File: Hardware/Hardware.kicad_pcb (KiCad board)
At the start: 2 copper layers, 58.4 x 30.5 mm, 16 parts, among them J1 Conn_01x02, J2 Conn_01x04, J3 Conn_01x06, J4 Conn_01x02, J7 Conn_01x03, U1 ESP32-WROOM-32

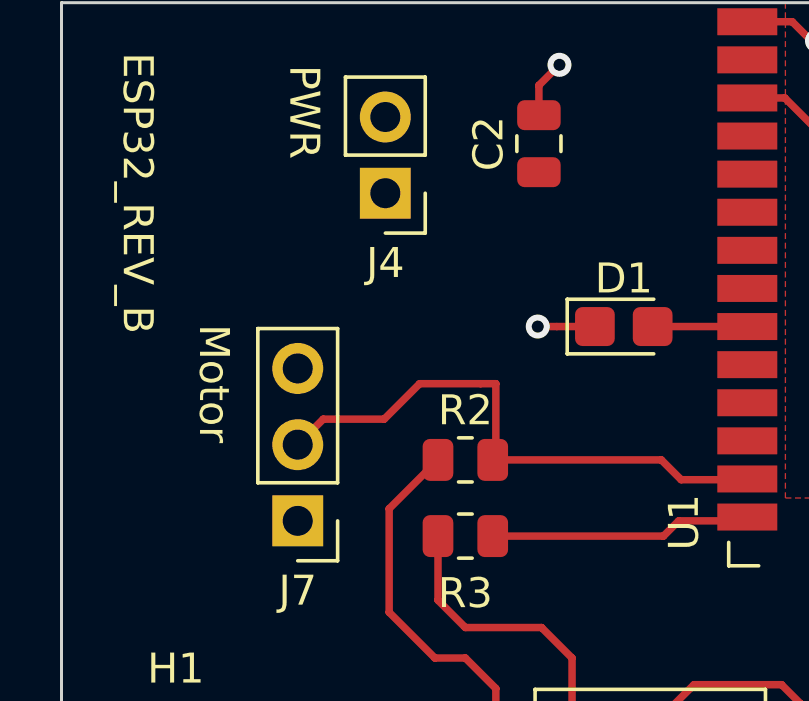
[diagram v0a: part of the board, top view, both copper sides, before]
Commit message: Servo pin fix
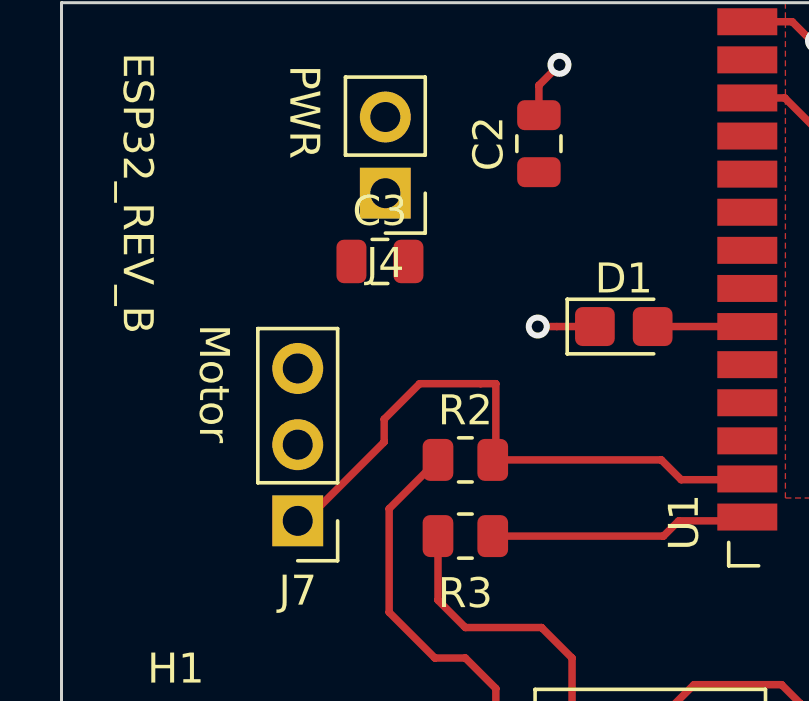
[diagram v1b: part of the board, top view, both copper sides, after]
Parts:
- added C3: 0.1uF, Capacitor_SMD:C_0805_2012Metric, F.Cu at (90.6, 105.1)
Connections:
- J7 pad 1: /VDD33 -> /MTMS
- J7 pad 2: /MTMS -> /VDD33
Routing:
- net /MTMS: track 18.6 -> 19.6 mm

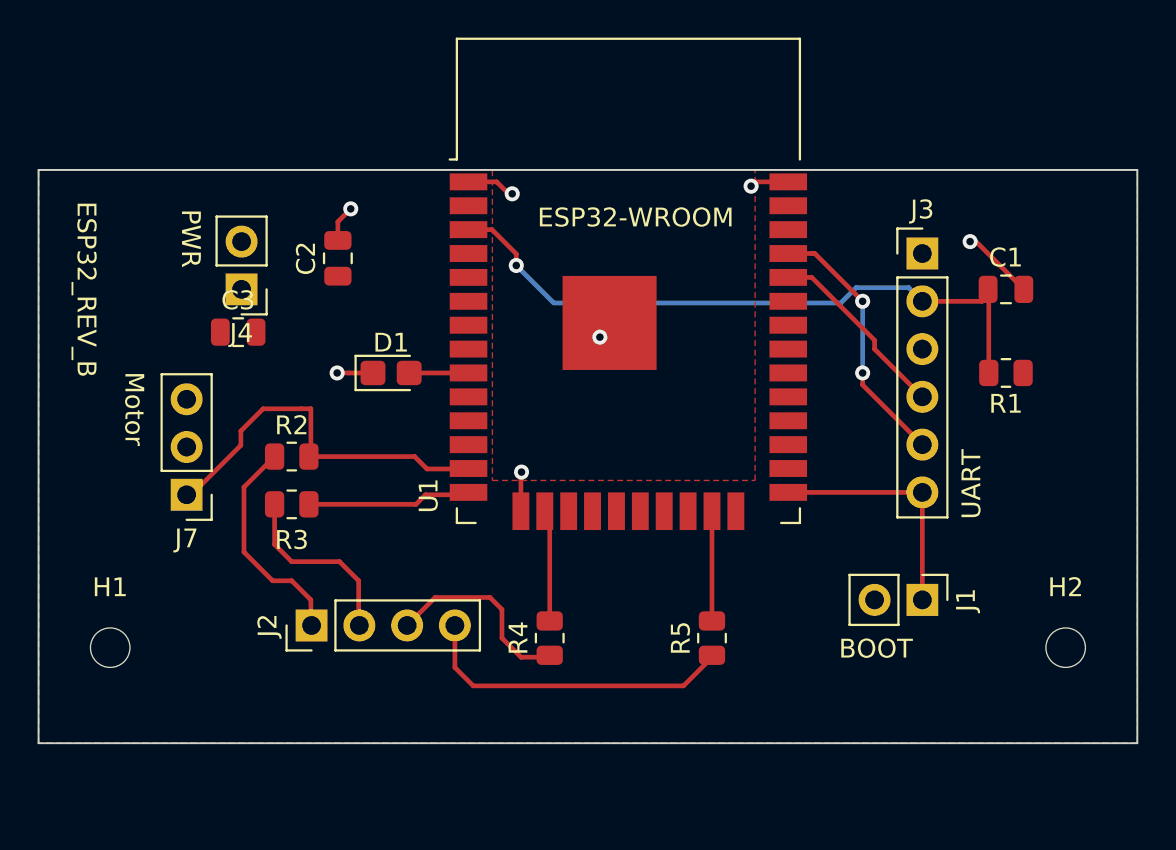
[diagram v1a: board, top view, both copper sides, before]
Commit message: Voltage regulator & power drop testing
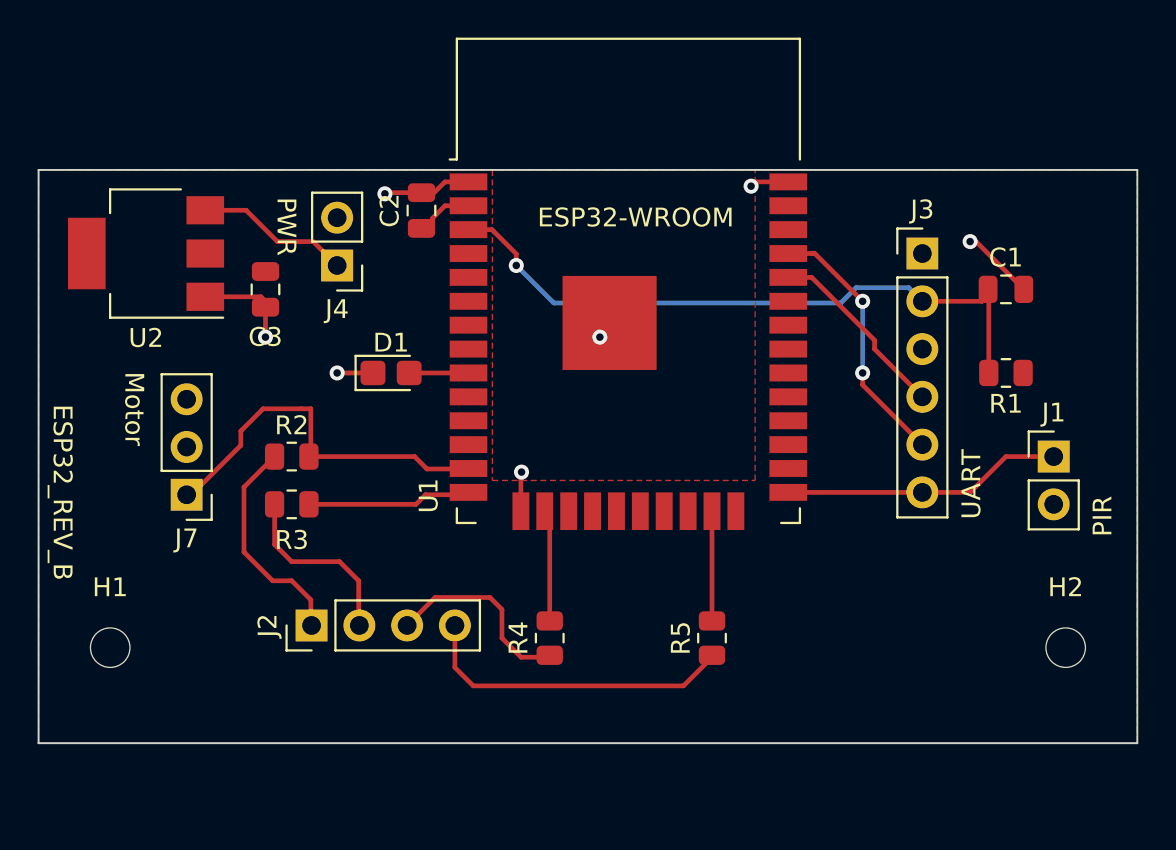
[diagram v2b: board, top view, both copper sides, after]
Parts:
- added U2: AMS1117-3.3, Package_TO_SOT_SMD:SOT-223-3_TabPin2, F.Cu at (85.7, 101.0)
- moved J1 10.3 mm to (134.0, 111.8), turned to 0 degrees
- moved J4 5.24 mm to (95.9, 101.6)
- moved C2 5.12 mm to (100.4, 98.7)
- moved C3 2.70 mm to (92.1, 102.9), turned to 270 degrees
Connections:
- net /Boot_Option renamed /PIR_INPUT
- J4 pad 1: /VDD33 -> Net-(J4-Pad1)
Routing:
- net Net-(J4-Pad1): track 0.00 -> 8.23 mm
- net GND: track 16.1 -> 21.9 mm
- net /VDD33: track 0.47 -> 3.26 mm
- net /PIR_INPUT: track 12.8 -> 14.9 mm
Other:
- board text added: "PIR"
- board text removed: "BOOT"

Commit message: Decoupling cap fix & servo power rewire
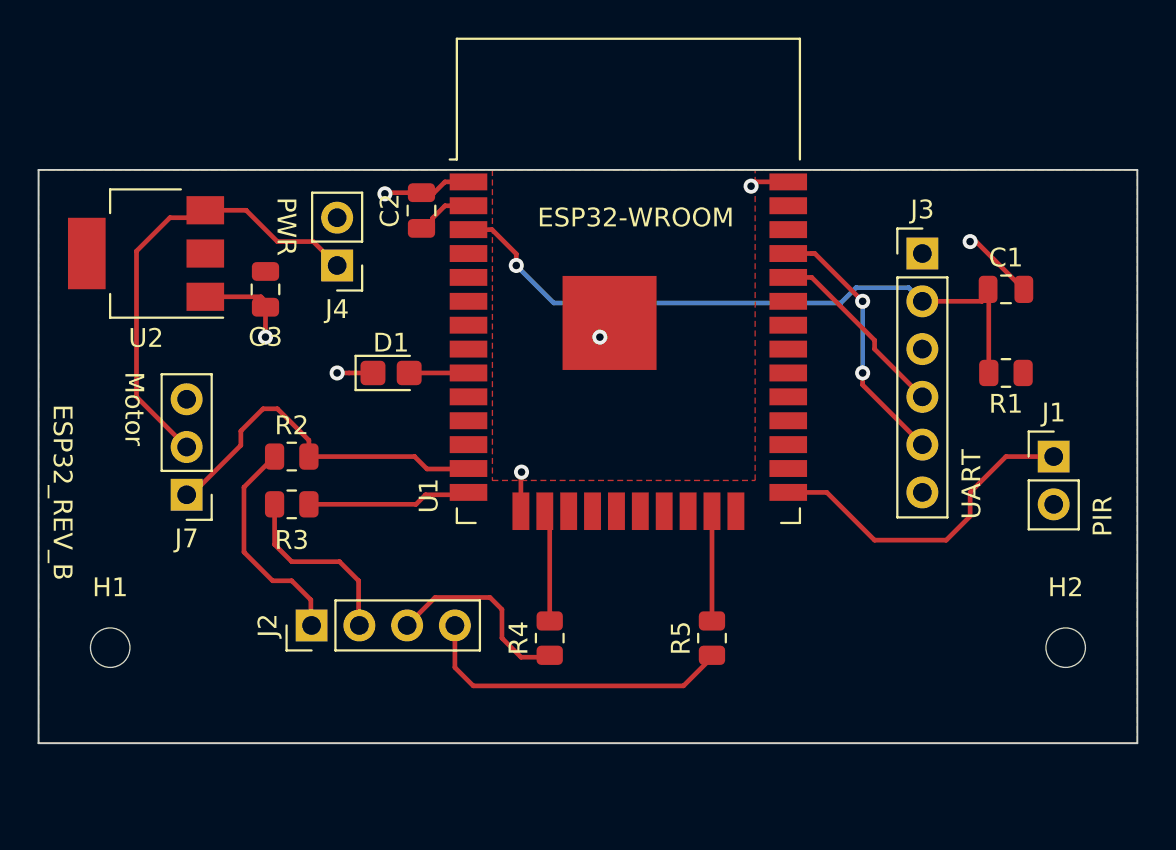
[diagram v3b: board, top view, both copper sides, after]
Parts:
- C2: value 10uF -> 1uF
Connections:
- J3 pad 6: /PIR_INPUT -> (no net)
- J4 pad 1: Net-(J4-Pad1) -> /BATT_POS
- J7 pad 2: /VDD33 -> /BATT_POS
- U2 pad 3: Net-(J4-Pad1) -> /BATT_POS
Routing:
- net /BATT_POS: track 0.00 -> 24.2 mm
- net Net-(J4-Pad1): track 8.23 -> 0.00 mm
- net /PIR_INPUT: track 14.9 -> 17.6 mm
- net /MTMS: track 19.6 -> 18.5 mm

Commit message: Barrel jack was added to board
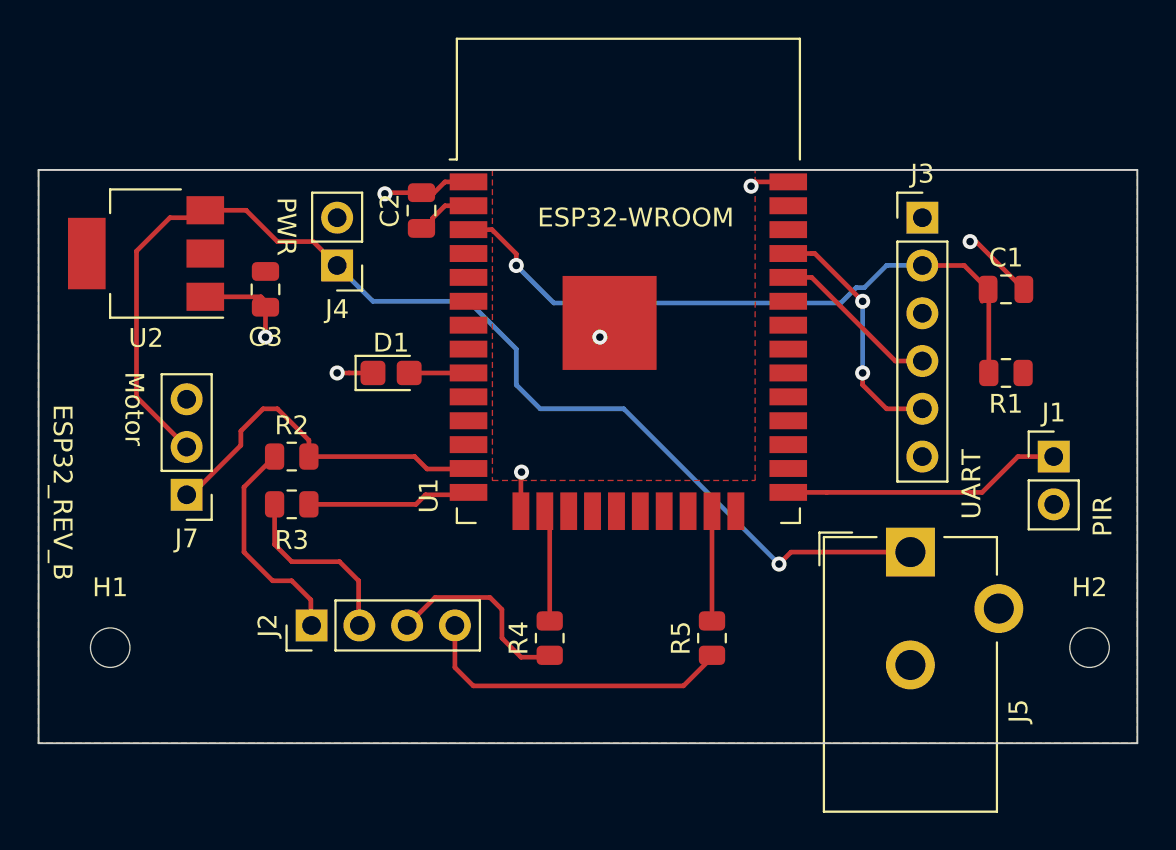
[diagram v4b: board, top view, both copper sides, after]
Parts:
- added J5: Jack-DC, Connector_BarrelJack:BarrelJack_CUI_PJ-102AH_Horizontal, F.Cu at (126.4, 116.8)
- moved J3 1.91 mm to (127.0, 99.1)
- moved H2 1.27 mm to (135.9, 121.9)
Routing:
- net /BATT_POS: track 24.2 -> 62.0 mm, vias 0 -> 1
- net /PIR_INPUT: track 17.6 -> 14.8 mm
- net /RXD: track 10.7 -> 9.59 mm
- net /EN: track 35.0 -> 36.1 mm
- net /TXD: track 13.9 -> 13.2 mm
